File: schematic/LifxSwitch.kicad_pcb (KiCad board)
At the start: 2 copper layers, 34 parts, among them J1 Serial, J2 Expansion, J3 USB_A, J4 CP_Expansion, J5 Arcade, U1 TouchStrip, U2 CP2102N-A01-GQFN20, U3 IQS572, U4 ESP-12E

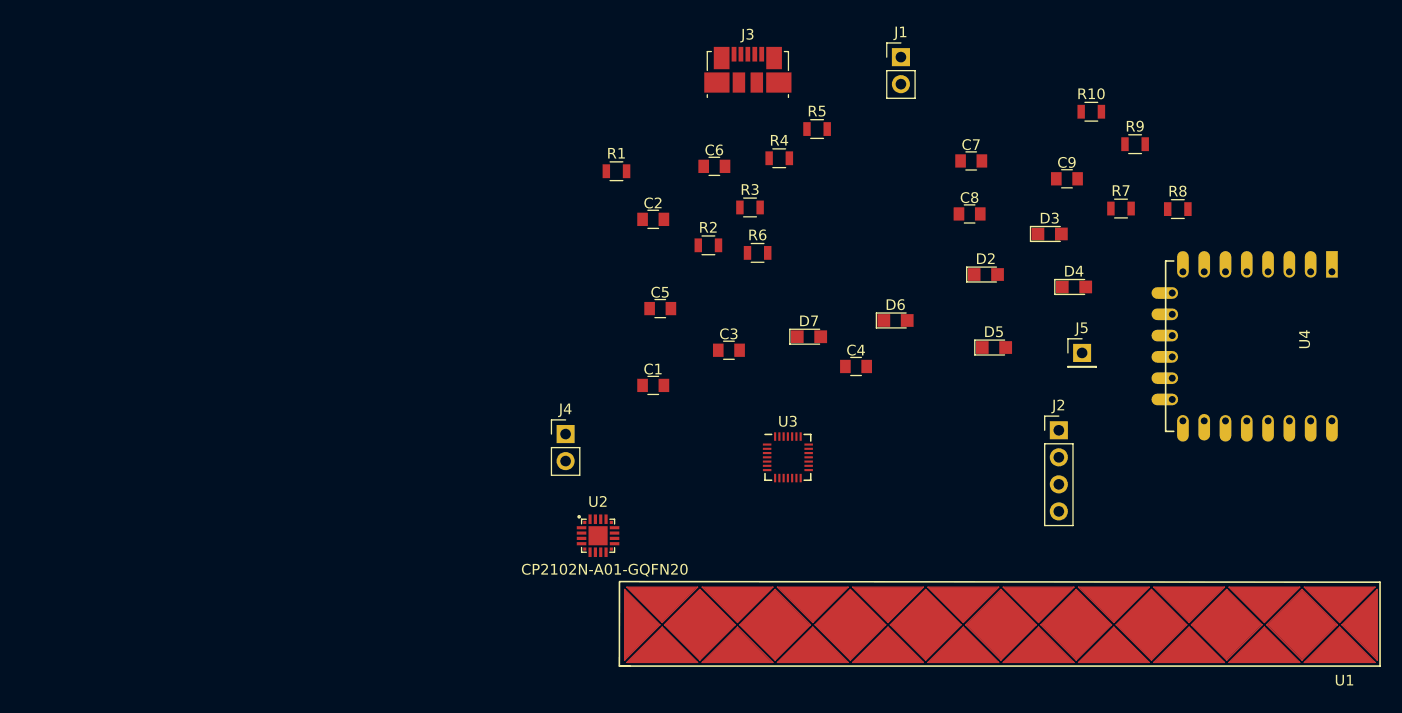
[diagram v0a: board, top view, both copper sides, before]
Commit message: Completed PCB layout
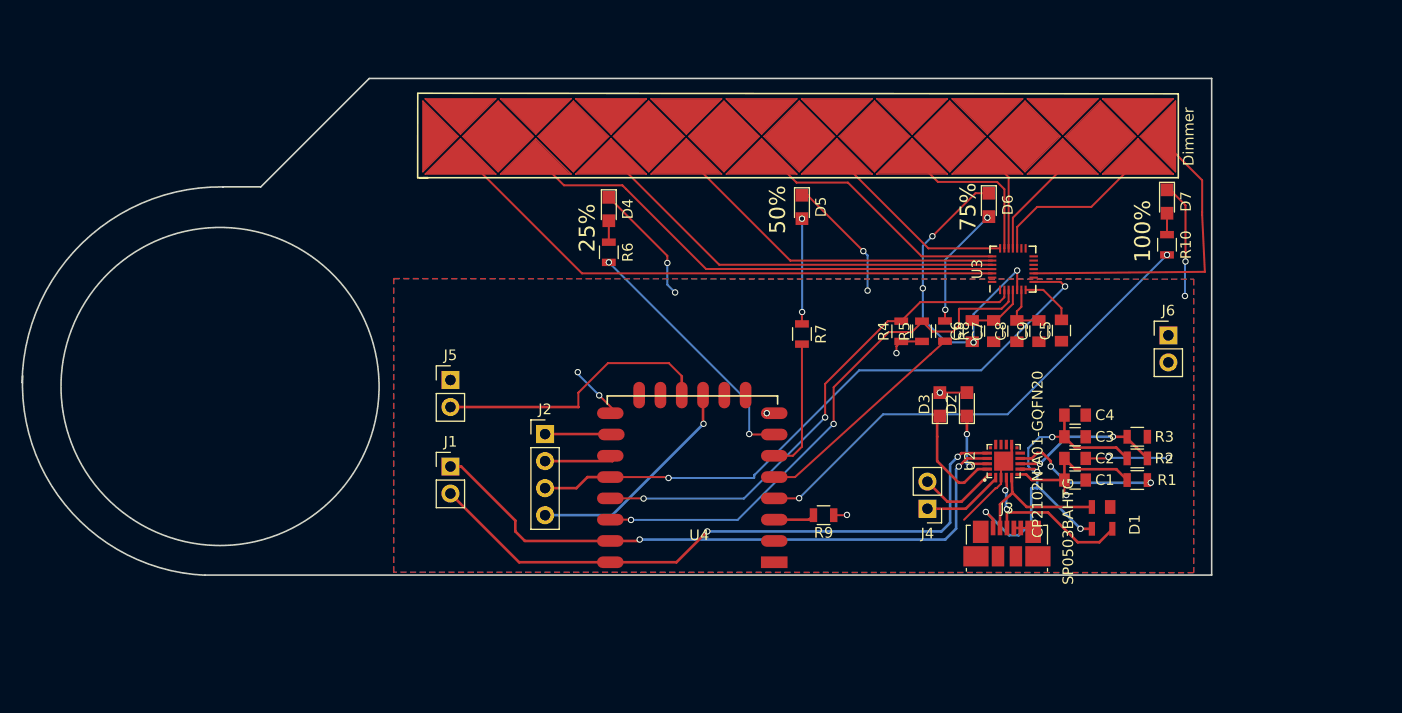
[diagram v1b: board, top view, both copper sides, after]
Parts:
- removed U1: TouchStrip, Buttons_Switches_SMD:Touchstrip
- added D1: SP0503BAHTG, SP0503BAHTG:SOT192P237X122-4N, F.Cu at (172.0, 131.3)
- added Dimmer: TouchStrip, Buttons_Switches_SMD:Touchstrip, F.Cu at (143.5, 95.5)
- added J6: Power, Pin_Headers:Pin_Header_Straight_1x02_Pitch2.54mm, F.Cu at (178.2, 114.2)
- J5: footprint Pin_Headers:Pin_Header_Straight_1x01_Pitch2.54mm -> Pin_Headers:Pin_Header_Straight_1x02_Pitch2.54mm
- R10, R6, R7, R8: value R -> 55
- moved U4 59.7 mm to (140.5, 135.5), turned to 180 degrees
- moved J5 59.4 mm to (110.7, 118.4)
- moved J1 57.2 mm to (110.7, 126.5)
- moved R1 56.9 mm to (175.3, 127.8)
- moved J3 50.7 mm to (163.0, 134.9)
- moved J2 48.3 mm to (119.6, 123.4)
- moved C2 45.5 mm to (169.4, 125.7), turned to 180 degrees
- moved R9 45.5 mm to (145.8, 131.1), turned to 180 degrees
- moved R2 45.0 mm to (175.3, 125.7)
- moved D4 44.3 mm to (125.6, 102.3), turned to 270 degrees
- moved R3 42.3 mm to (175.3, 123.7)
- moved C1 40.6 mm to (169.4, 127.8), turned to 180 degrees
- moved U2 38.7 mm to (162.7, 126.0), turned to 90 degrees
- moved C5 37.7 mm to (168.1, 113.7), turned to 90 degrees
- moved D7 35.9 mm to (178.1, 101.6), turned to 270 degrees
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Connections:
- J3 pad 6: (no net) -> VSS
- J5 pad 1: LightStatus -> VSS
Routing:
- net VSS: track 0.00 -> 89.7 mm, vias 0 -> 14
- net TX: track 0.00 -> 60.6 mm, vias 0 -> 2
- net RX: track 0.00 -> 60.4 mm, vias 0 -> 2
- net Gpio0: track 0.00 -> 60.1 mm, vias 0 -> 2
- net Net-(U1-Pad10): track 0.00 -> 54.5 mm
- net Net-(R5-Pad2): track 0.00 -> 50.1 mm, vias 0 -> 2
- net Net-(U1-Pad9): track 0.00 -> 47.2 mm
- net 100: track 0.00 -> 47.1 mm, vias 0 -> 2
- net Net-(R4-Pad2): track 0.00 -> 46.7 mm, vias 0 -> 2
- net Net-(U1-Pad8): track 0.00 -> 40.0 mm
- net +5V: track 0.00 -> 36.9 mm, vias 0 -> 4
- net Net-(U1-Pad7): track 0.00 -> 32.8 mm
- net Net-(U1-Pad1): track 0.00 -> 30.5 mm
- net LightStatus: track 0.00 -> 27.5 mm
- net Net-(U1-Pad6): track 0.00 -> 25.5 mm
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- added copper zone on B.Cu, net +3V3
- added copper zone on F.Cu, net VSS
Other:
- board outline added: 111.7 x 46.7 mm
- net class Default: clearance 0.2 -> 0.18; trace_width 0.25 -> 0.19
- rule trace_clearance: 0.2 -> 0.18
- rule trace_min: 0.2 -> 0.18
- board text added: "100%"
- board text added: "25%"
- board text added: "50%"
- board text added: "75%"

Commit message: Finished V1 schematic
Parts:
- added C10: 10uF, Capacitors_SMD:C_0805, F.Cu at (140.5, 116.2)
- added C11: 0.1uF, Capacitors_SMD:C_0805, F.Cu at (138.4, 116.2)
- added REF***: OSHW-Logo_5.7x6mm_SilkScreen, Symbols:OSHW-Logo_5.7x6mm_SilkScreen, F.Cu at (102.3, 132.7)
- J5: footprint Pin_Headers:Pin_Header_Straight_1x02_Pitch2.54mm -> Pin_Headers:Pin_Header_Straight_1x04_Pitch2.54mm
- moved J5 0.61 mm to (110.7, 119.0), turned to 180 degrees
- renumbered D2 to RX, D3 to TX
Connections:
- J3 pad 6: VSS -> (no net)
- J5 pad 2: LightStatus -> VSS
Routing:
- net Gpio15: track 6.84 -> 21.8 mm
- net +3V3: track 22.0 -> 28.5 mm, vias 5 -> 6
- net VSS: track 89.7 -> 95.5 mm
- net LightStatus: track 27.5 -> 26.8 mm
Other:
- board text added: "+"
- board text added: "-"
- board text added: "Button"
- board text added: "ESP8266"
- board text added: "G0"
- board text added: "G1"
- board text added: "IO0"
- board text added: "IO15"
- board text added: "IO2"
- board text added: "IO9"
- board text added: "Light"
- board text added: "RX"
- board text added: "Smart Switch"
- board text added: "TX"
- board text added: "WR"
